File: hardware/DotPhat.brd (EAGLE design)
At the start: 30 x 65 mm, 57 parts, among them CN1 1X4-BIG, IC1 CAT24M010TS, IC3 SI1145, J3 USB-MICROB, Q1 BSH103, U1 ATMEGA328P-MU-QFN32, U2 TMP102, U3 ATSHA204-TSU, X2 MC-RTC-RV-4162-C7-I2C, X3 S4B-ZR

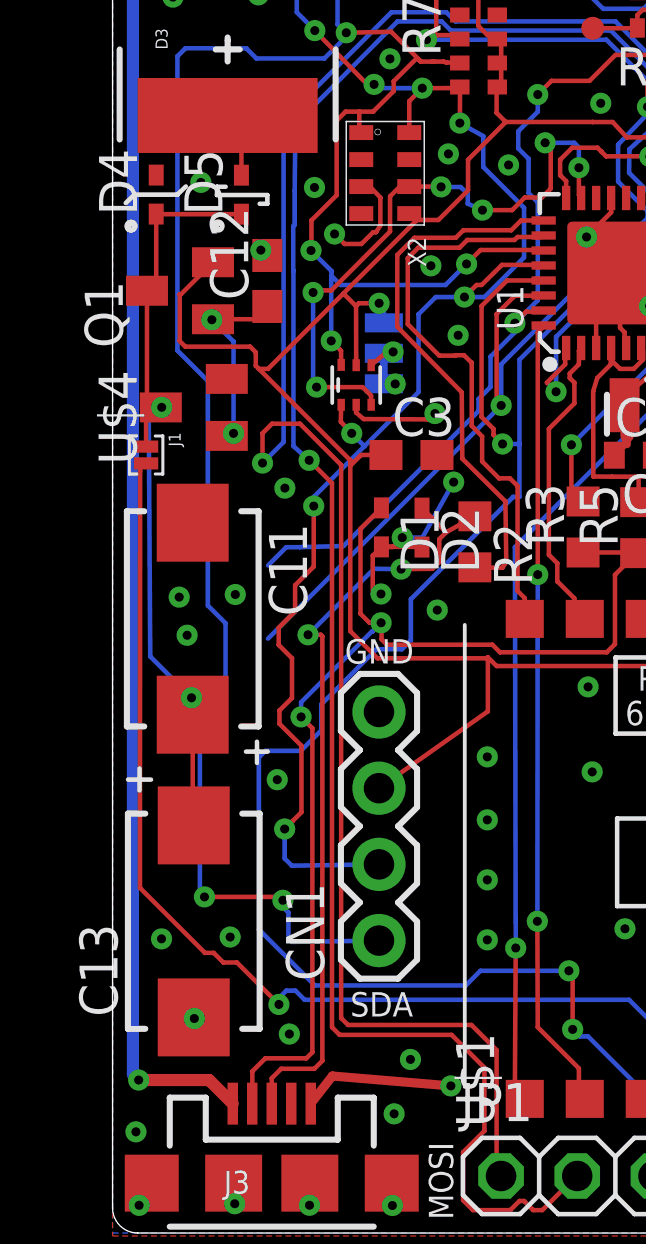
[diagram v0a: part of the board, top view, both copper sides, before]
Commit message: Add 3rd solar cap
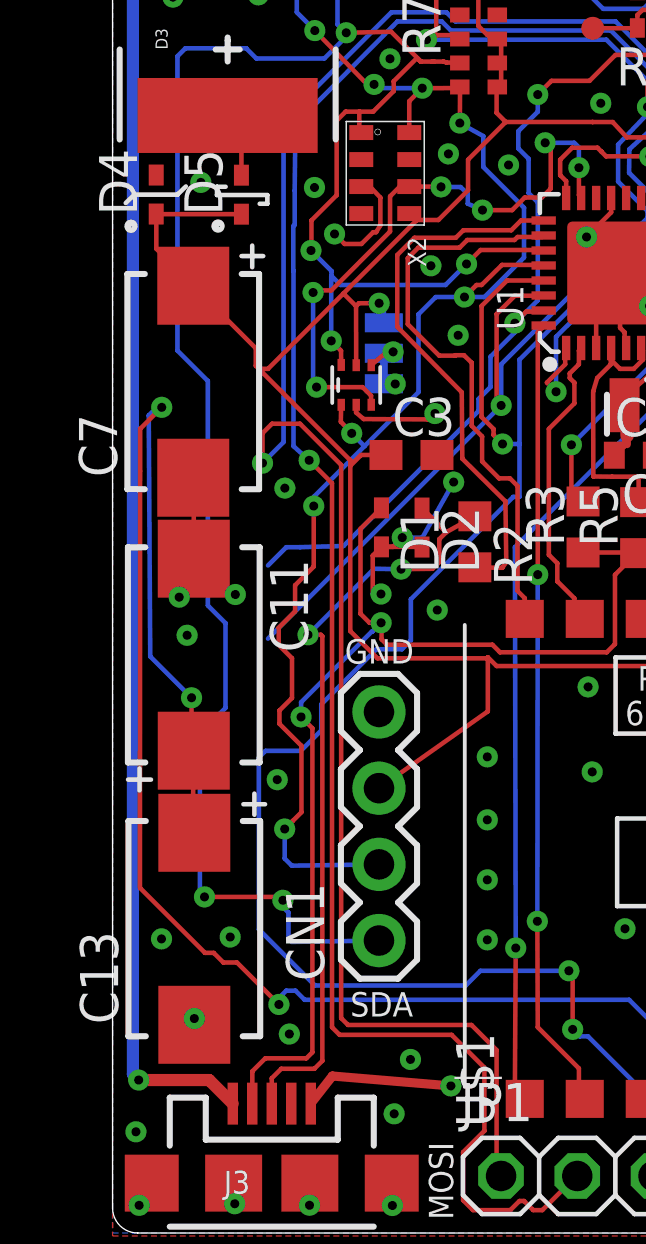
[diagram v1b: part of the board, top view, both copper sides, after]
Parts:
- removed C12: 1uF 4V, rcl:C0603
- removed J1: (no value), solderjumper:2.MED
- removed Q1: BSH103, adafruit:SOT23
- removed U$4: AD1582, AD1582:SOT23
- added C7: 1500uF 4V, adafruit:CT7343
- moved C11 1.20 mm to (2.71, 19.3)
- moved C13 0.25 mm to (2.73, 10.1)
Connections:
- removed net CAPS_VCC: C11.+, C13.+, D4.C, D5.C, J1.1, Q1.3, U$4.3
- removed net MOSFET: C12.1, Q1.1, U$4.1
- net +3V3: now also C11.+, C13.+, C7.+, D4.C, D5.C; no longer J1.2, Q1.2
- net GND: now also C7.-; no longer C12.2, U$4.2
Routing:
- net CAPS_VCC: track 27.2 -> 0.00 mm, vias 2 -> 0
- net +3V3: track 234.3 -> 254.2 mm, vias 9 -> 11
- net MOSFET: track 6.37 -> 0.00 mm, vias 2 -> 0
- net GND: track 41.9 -> 44.4 mm, vias 145 -> 144
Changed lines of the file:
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@@
 <circle x="3.516" y="33.564" radius="0.146453125" width="0.1524" layer="21"/>
 <circle x="3.557" y="33.546" radius="0.055971875" width="0.1524" layer="21"/>
-<wire x1="4.448" y1="16.045" x2="5.171" y2="16.045" width="0.1524" layer="21"/>
-<wire x1="4.813" y1="16.376" x2="4.813" y2="15.67" width="0.1524" layer="21"/>
+<wire x1="4.361" y1="14.291" x2="5.084" y2="14.291" width="0.1524" layer="21"/>
+<wire x1="4.728" y1="14.647" x2="4.728" y2="13.941" width="0.1524" layer="21"/>
 <wire x1="0.516" y1="15.113" x2="1.282" y2="15.113" width="0.1524" layer="21"/>
 <wire x1="0.901" y1="15.486" x2="0.901" y2="14.752" width="0.1524" layer="21"/>
+<wire x1="4.299" y1="32.564" x2="5.022" y2="32.564" width="0.1524" layer="21"/>
+<wire x1="4.655" y1="32.191" x2="4.655" y2="32.914" width="0.1524" layer="21"/>
 </plain>
 <attributes>
@@
 <element name="D3" library="SparkFun" package="SOLARBIT-12X1" value="Solar Cell 4V" x="3.837" y="47.45" rot="R90"/>
 <element name="D4" library="diode" package="SOD523" value="3.6V Zener" x="1.455" y="34.564" rot="R90"/>
-<element name="C11" library="adafruit" package="CT7343" value="1500uF 4V" x="2.672" y="20.476" rot="R270"/>
-<element name="C13" library="adafruit" package="CT7343" value="1500uF 4V" x="2.707" y="10.387" rot="R90"/>
+<element name="C11" library="adafruit" package="CT7343" value="1500uF 4V" x="2.707" y="19.276" rot="R270"/>
+<element name="C13" library="adafruit" package="CT7343" value="1500uF 4V" x="2.725" y="10.14" rot="R90"/>
 <element name="D5" library="diode" package="SOD523" value="0.3V Schottky" x="4.296" y="34.56" rot="R90"/>
-<element name="Q1" library="adafruit" package="SOT23" value="BSH103" x="2.247" y="31.408" rot="R90"/>
-<element name="U$4" library="AD1582" package="SOT23" value="AD1582" x="2.708" y="27.519" rot="R90"/>
-<element name="C12" library="rcl" package="C0603" value="1uF 4V" x="5.158" y="31.734" rot="R90"/>
 <element name="IC3" library="silabs" package="QFN-10" value="SI1145" x="15.201" y="50.892"/>
 <element name="TP1" library="SparkFun" package="PAD.03X.03" value="TEST-POINT3" x="16.006" y="40.157"/>
-<element name="J1" library="solderjumper" package="2.MED" value="" x="1.117" y="25.933" rot="R270"/>
+<element name="C7" library="adafruit" package="CT7343" value="1500uF 4V" x="2.69" y="28.375" rot="R90"/>
 </elements>
 <signals>
@@
 <contactref element="D4" pad="A"/>
 <wire x1="1.13365625" y1="63.929865625" x2="1.6" y2="64.396209375" width="0.1524" layer="16"/>
-<contactref element="U$4" pad="2"/>
-<contactref element="C12" pad="2"/>
 <contactref element="IC3" pad="8"/>
 <via x="5.893209375" y="6.631765625" extent="1-16" drill="0.3"/>
 <via x="6.731" y="34.85" extent="1-16" drill="0.3"/>
 <via x="2.943" y="35.02" extent="1-16" drill="0.3"/>
-<via x="4.942" y="32.762" extent="1-16" drill="0.3"/>
-<wire x1="5.158" y1="32.584" x2="4.98" y2="32.762" width="0.1524" layer="1"/>
-<wire x1="4.98" y1="32.762" x2="4.942" y2="32.762" width="0.1524" layer="1"/>
 <wire x1="8.29" y1="34.88" x2="8.581" y2="34.88" width="0.1524" layer="1"/>
 <wire x1="8.296" y1="32.967" x2="7.733" y2="32.967" width="0.1524" layer="1"/>
@@
 <via x="11.480859375" y="53.973615625" extent="1-16" drill="0.3"/>
 <via x="14.073859375" y="48.023615625" extent="1-16" drill="0.3"/>
+<contactref element="C7" pad="-"/>
+<wire x1="2.69" y1="25.175" x2="2.707" y2="25.175" width="0.1524" layer="1"/>
+<wire x1="2.707" y1="25.175" x2="2.707" y2="22.476" width="0.1524" layer="1"/>
 </signal>
 <signal name="SDA">
@@
 <wire x1="21.345" y1="46.29" x2="21.345" y2="45.21" width="0.1524" layer="1"/>
 <wire x1="21.345" y1="45.21" x2="22.125" y2="44.43" width="0.1524" layer="1"/>
-<contactref element="Q1" pad="2"/>
 <contactref element="IC3" pad="3"/>
 <wire x1="19.478" y1="61.722" x2="19.472159375" y2="61.727840625" width="0.1524" layer="1"/>
-<wire x1="3.347" y1="32.358" x2="2.277" y2="31.288" width="0.1524" layer="1"/>
-<wire x1="2.277" y1="31.288" x2="2.238" y2="31.288" width="0.1524" layer="1"/>
-<wire x1="2.238" y1="31.288" x2="2.238" y2="29.731" width="0.1524" layer="1"/>
-<wire x1="2.238" y1="29.731" x2="2.425" y2="29.544" width="0.1524" layer="1"/>
-<wire x1="2.425" y1="29.544" x2="4.587" y2="29.544" width="0.1524" layer="1"/>
-<wire x1="4.587" y1="29.544" x2="4.774" y2="29.357" width="0.1524" layer="1"/>
-<wire x1="4.774" y1="29.357" x2="4.774" y2="28.9064" width="0.1524" layer="1"/>
 <wire x1="4.774" y1="28.9064" x2="4.8768" y2="28.8036" width="0.1524" layer="1"/>
 <wire x1="14.301" y1="50.642" x2="14.29" y2="50.631" width="0.1524" layer="1"/>
@@
 <wire x1="13.337" y1="50.631" x2="13.01" y2="50.304" width="0.1524" layer="1"/>
 <wire x1="13.01" y1="50.304" x2="13.01" y2="46.375" width="0.1524" layer="1"/>
-<contactref element="J1" pad="2"/>
-<wire x1="1.117" y1="25.6536" x2="1.117" y2="25.595" width="0.1524" layer="1"/>
 <wire x1="0.919" y1="25.397" x2="0.913" y2="11.505" width="0.1524" layer="1"/>
 <wire x1="0.913" y1="11.505" x2="3.081" y2="9.337" width="0.1524" layer="1"/>
@@
 <wire x1="5.545" y1="7.618" x2="5.545" y2="7.831" width="0.1524" layer="16"/>
 <wire x1="5.545" y1="7.831" x2="5.7912" y2="8.0772" width="0.1524" layer="16"/>
-<wire x1="0.919" y1="25.397" x2="0.919" y2="25.6536" width="0.1524" layer="1"/>
-<wire x1="0.919" y1="25.6536" x2="1.117" y2="25.6536" width="0.1524" layer="1"/>
+<contactref element="C13" pad="+"/>
+<contactref element="C11" pad="+"/>
+<contactref element="D5" pad="C"/>
+<contactref element="D4" pad="C"/>
+<contactref element="C7" pad="+"/>
+<wire x1="4.296" y1="33.96" x2="1.459" y2="33.96" width="0.1524" layer="1"/>
+<wire x1="1.459" y1="33.96" x2="1.455" y2="33.964" width="0.1524" layer="1"/>
+<via x="1.639" y="27.522" extent="1-16" drill="0.3"/>
+<wire x1="1.639" y1="27.522" x2="1.475" y2="27.522" width="0.1524" layer="16"/>
+<wire x1="1.475" y1="27.522" x2="1.206" y2="27.253" width="0.1524" layer="16"/>
+<wire x1="1.206" y1="27.253" x2="1.256" y2="19.217" width="0.1524" layer="16"/>
+<wire x1="1.256" y1="19.217" x2="2.633" y2="17.84" width="0.1524" layer="16"/>
+<via x="2.633" y="17.84" extent="1-16" drill="0.3"/>
+<wire x1="2.633" y1="17.84" x2="2.633" y2="17.315" width="0.1524" layer="1"/>
+<wire x1="2.633" y1="17.315" x2="2.707" y2="16.076" width="0.1524" layer="1"/>
+<wire x1="2.707" y1="16.076" x2="2.672" y2="13.622" width="0.1524" layer="1"/>
+<wire x1="2.672" y1="13.622" x2="2.725" y2="13.34" width="0.1524" layer="1"/>
+<wire x1="0.919" y1="25.397" x2="0.919" y2="26.802" width="0.1524" layer="1"/>
+<wire x1="0.919" y1="26.802" x2="1.639" y2="27.522" width="0.1524" layer="1"/>
+<wire x1="4.774" y1="28.9064" x2="4.774" y2="29.491" width="0.1524" layer="1"/>
+<wire x1="4.774" y1="29.491" x2="2.69" y2="31.575" width="0.1524" layer="1"/>
+<wire x1="1.459" y1="33.96" x2="1.459" y2="32.806" width="0.1524" layer="1"/>
+<wire x1="1.459" y1="32.806" x2="2.69" y2="31.575" width="0.1524" layer="1"/>
 <wire x1="9.26490625" y1="59.71336875" x2="9.6006" y2="59.71" width="0" layer="19" extent="1-1"/>
 </signal>
@@
 <wire x1="22.845" y1="46.115" x2="22.11" y2="45.38" width="0.1524" layer="1"/>
 </signal>
-<signal name="CAPS_VCC">
-<contactref element="C13" pad="+"/>
-<contactref element="C11" pad="+"/>
-<contactref element="U$4" pad="3"/>
-<contactref element="D5" pad="C"/>
-<contactref element="D4" pad="C"/>
-<contactref element="Q1" pad="3"/>
-<wire x1="4.296" y1="33.96" x2="1.459" y2="33.96" width="0.1524" layer="1"/>
-<wire x1="1.459" y1="33.96" x2="1.455" y2="33.964" width="0.1524" layer="1"/>
-<wire x1="1.455" y1="33.964" x2="1.455" y2="31.716" width="0.1524" layer="1"/>
-<wire x1="1.455" y1="31.716" x2="1.147" y2="31.408" width="0.1524" layer="1"/>
-<wire x1="1.147" y1="31.408" x2="1.147" y2="27.643" width="0.1524" layer="1"/>
-<wire x1="1.147" y1="27.643" x2="1.608" y2="27.519" width="0.1524" layer="1"/>
-<wire x1="1.608" y1="27.519" x2="1.261" y2="27.342" width="0.1524" layer="1"/>
-<wire x1="1.261" y1="27.342" x2="1.639" y2="27.522" width="0.1524" layer="1"/>
-<via x="1.639" y="27.522" extent="1-16" drill="0.3"/>
-<wire x1="1.639" y1="27.522" x2="1.475" y2="27.522" width="0.1524" layer="16"/>
-<wire x1="1.475" y1="27.522" x2="1.206" y2="27.253" width="0.1524" layer="16"/>
-<wire x1="1.206" y1="27.253" x2="1.256" y2="19.217" width="0.1524" layer="16"/>
-<wire x1="1.256" y1="19.217" x2="2.633" y2="17.84" width="0.1524" layer="16"/>
-<via x="2.633" y="17.84" extent="1-16" drill="0.3"/>
-<wire x1="2.633" y1="17.84" x2="2.633" y2="17.315" width="0.1524" layer="1"/>
-<wire x1="2.633" y1="17.315" x2="2.672" y2="17.276" width="0.1524" layer="1"/>
-<wire x1="2.672" y1="17.276" x2="2.672" y2="13.622" width="0.1524" layer="1"/>
-<wire x1="2.672" y1="13.622" x2="2.707" y2="13.587" width="0.1524" layer="1"/>
-<contactref element="J1" pad="1"/>
-<wire x1="1.117" y1="26.2124" x2="1.117" y2="27.522" width="0.1524" layer="1"/>
-<wire x1="1.117" y1="27.522" x2="1.639" y2="27.522" width="0.1524" layer="1"/>
-</signal>
-<signal name="MOSFET">
-<contactref element="Q1" pad="1"/>
-<contactref element="U$4" pad="1"/>
-<contactref element="C12" pad="1"/>
-<wire x1="5.158" y1="30.884" x2="4.732" y2="30.458" width="0.1524" layer="1"/>
-<wire x1="4.732" y1="30.458" x2="3.347" y2="30.458" width="0.1524" layer="1"/>
-<wire x1="3.347" y1="30.458" x2="3.33" y2="30.441" width="0.1524" layer="1"/>
-<wire x1="3.33" y1="30.441" x2="3.309" y2="30.441" width="0.1524" layer="1"/>
-<via x="3.309" y="30.441" extent="1-16" drill="0.3"/>
-<wire x1="3.309" y1="30.441" x2="4.032" y2="29.718" width="0.1524" layer="16"/>
-<wire x1="4.032" y1="29.718" x2="4.032" y2="26.654" width="0.1524" layer="16"/>
-<via x="4.032" y="26.654" extent="1-16" drill="0.3"/>
-<wire x1="4.032" y1="26.654" x2="3.957" y2="26.579" width="0.1524" layer="1"/>
-<wire x1="3.957" y1="26.579" x2="3.808" y2="26.569" width="0.1524" layer="1"/>
-</signal>
 <signal name="N$5">

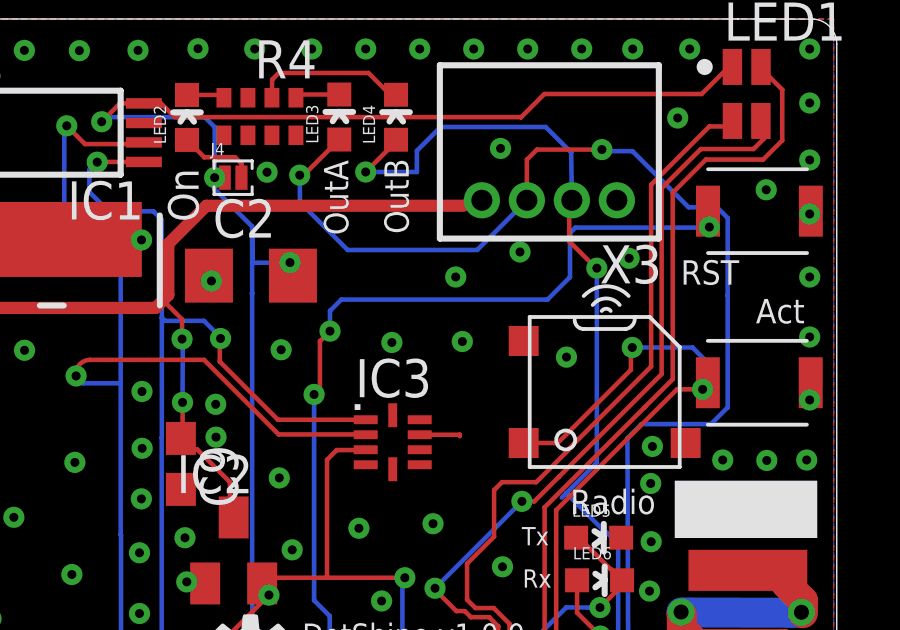
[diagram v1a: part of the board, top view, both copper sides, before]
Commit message: Add mount hole
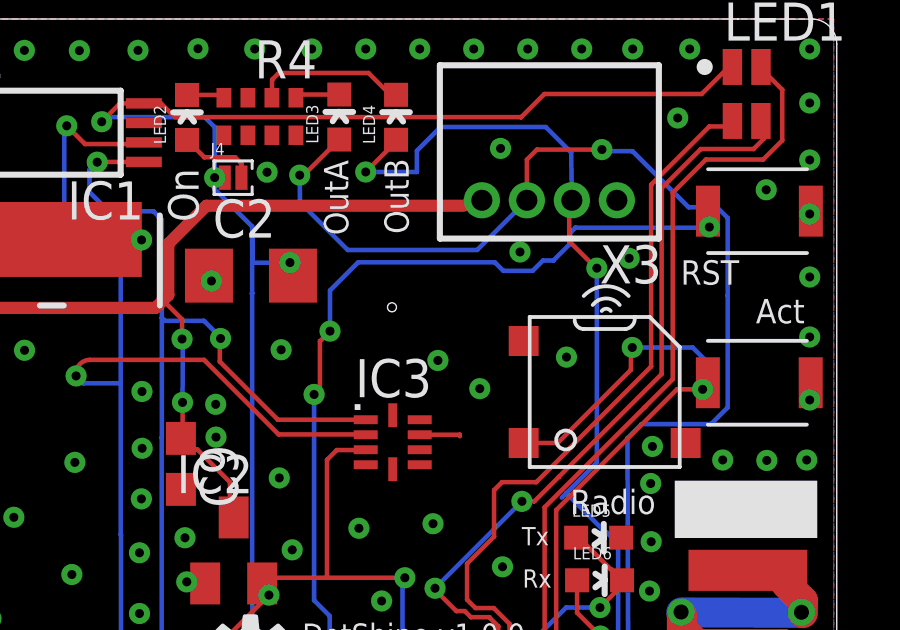
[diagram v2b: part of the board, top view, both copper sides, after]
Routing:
- net GND: vias 144 -> 143
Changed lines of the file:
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@@
 <layer number="43" name="vRestrict" color="2" fill="10" visible="yes" active="yes"/>
 <layer number="44" name="Drills" color="7" fill="1" visible="no" active="yes"/>
-<layer number="45" name="Holes" color="7" fill="1" visible="no" active="yes"/>
+<layer number="45" name="Holes" color="7" fill="1" visible="yes" active="yes"/>
 <layer number="46" name="Milling" color="3" fill="1" visible="yes" active="yes"/>
 <layer number="47" name="Measures" color="7" fill="1" visible="yes" active="yes"/>
@@
 <wire x1="4.299" y1="32.564" x2="5.022" y2="32.564" width="0.1524" layer="21"/>
 <wire x1="4.655" y1="32.191" x2="4.655" y2="32.914" width="0.1524" layer="21"/>
+<hole x="15.176" y="55.39" drill="0.3"/>
 </plain>
 <attributes>
@@
 <via x="25.1" y="64" extent="1-16" drill="0.3"/>
 <via x="24.7" y="61.7" extent="1-16" drill="0.3"/>
-<via x="17.3" y="56.4" extent="1-16" drill="0.3"/>
+<wire x1="17.3" y1="56.4" x2="17.3" y2="56.4" width="0" layer="19" extent="1-16"/>
 <via x="9.3" y="52.1556" extent="1-16" drill="0.3"/>
 <via x="11.520140625" y="29.9230625" extent="1-16" drill="0.3"/>
@@
 <via x="2.571859375" y="48.389615625" extent="1-16" drill="0.3"/>
 <via x="3.487859375" y="43.305615625" extent="1-16" drill="0.3"/>
-<via x="17.520859375" y="54.248615625" extent="1-16" drill="0.3"/>
+<via x="18.102859375" y="52.677615625" extent="1-16" drill="0.3"/>
 <via x="16.544859375" y="48.176615625" extent="1-16" drill="0.3"/>
-<via x="15.171859375" y="54.217615625" extent="1-16" drill="0.3"/>
+<via x="16.706859375" y="53.617615625" extent="1-16" drill="0.3"/>
 <via x="11.419859375" y="49.701615625" extent="1-16" drill="0.3"/>
 <via x="11.480859375" y="53.973615625" extent="1-16" drill="0.3"/>
@@
 <wire x1="12.775" y1="54.26" x2="13.11" y2="54.595" width="0.1524" layer="1"/>
 <via x="13.11" y="54.595" extent="1-16" drill="0.3"/>
-<wire x1="13.11" y1="54.595" x2="13.11" y2="55.27" width="0.1524" layer="16"/>
-<wire x1="13.11" y1="55.27" x2="13.485" y2="55.645" width="0.1524" layer="16"/>
-<wire x1="13.485" y1="55.645" x2="20.36" y2="55.645" width="0.1524" layer="16"/>
-<wire x1="20.36" y1="55.645" x2="21.11" y2="56.395" width="0.1524" layer="16"/>
-<wire x1="21.11" y1="56.395" x2="21.11" y2="57.86506875" width="0.1524" layer="16"/>
+<wire x1="21.11" y1="56.395" x2="21.11" y2="57.5" width="0" layer="19" extent="1-16"/>
+<wire x1="21.11" y1="57.5" x2="21.11" y2="57.86506875" width="0.1524" layer="16"/>
 <wire x1="21.11" y1="57.86506875" x2="21.29028125" y2="58.04535" width="0.1524" layer="16"/>
 <wire x1="12.58" y1="52.485" x2="12.58" y2="45.62" width="0.1524" layer="16"/>
@@
 <wire x1="8.795" y1="19.458" x2="9.645471875" y2="19.458" width="0.1524" layer="16"/>
 <wire x1="9.645471875" y1="19.458" x2="9.943846875" y2="19.756375" width="0.1524" layer="16"/>
+<wire x1="13.11" y1="54.595" x2="13.11" y2="55.952" width="0.1524" layer="16"/>
+<wire x1="13.11" y1="55.952" x2="14.045" y2="56.887" width="0.1524" layer="16"/>
+<wire x1="14.045" y1="56.887" x2="18.605" y2="56.887" width="0.1524" layer="16"/>
+<wire x1="18.605" y1="56.887" x2="18.887" y2="56.605" width="0.1524" layer="16"/>
+<wire x1="18.887" y1="56.605" x2="19.867" y2="56.605" width="0.1524" layer="16"/>
+<wire x1="19.867" y1="56.605" x2="20.21" y2="56.948" width="0.1524" layer="16"/>
+<wire x1="20.21" y1="56.948" x2="20.558" y2="56.948" width="0.1524" layer="16"/>
+<wire x1="20.558" y1="56.948" x2="21.11" y2="57.5" width="0.1524" layer="16"/>
 </signal>
 <signal name="LED">
